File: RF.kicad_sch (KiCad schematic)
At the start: 5 parts, among them U9 SAM-M10Q-00B

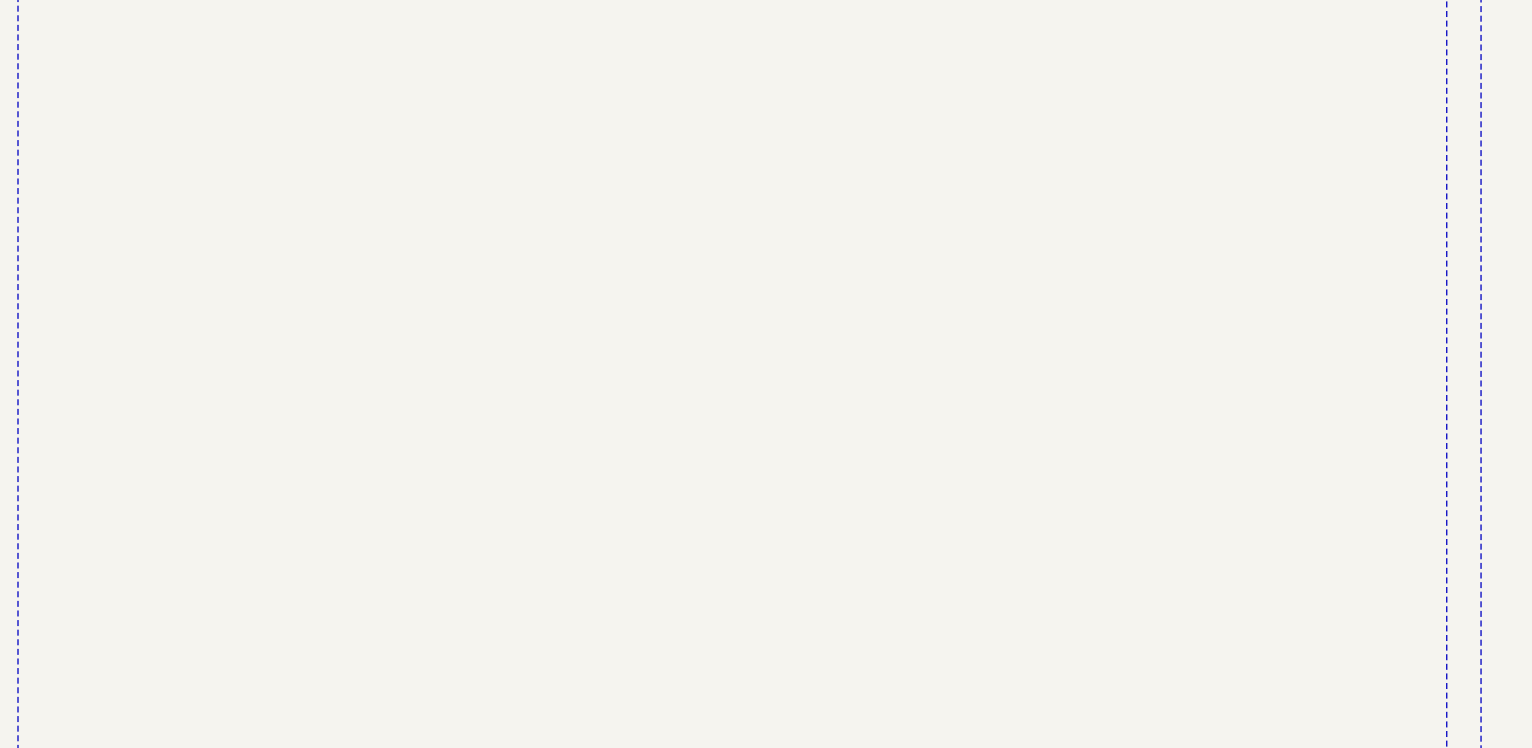
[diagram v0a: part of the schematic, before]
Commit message: added Buzzer, status LEDs
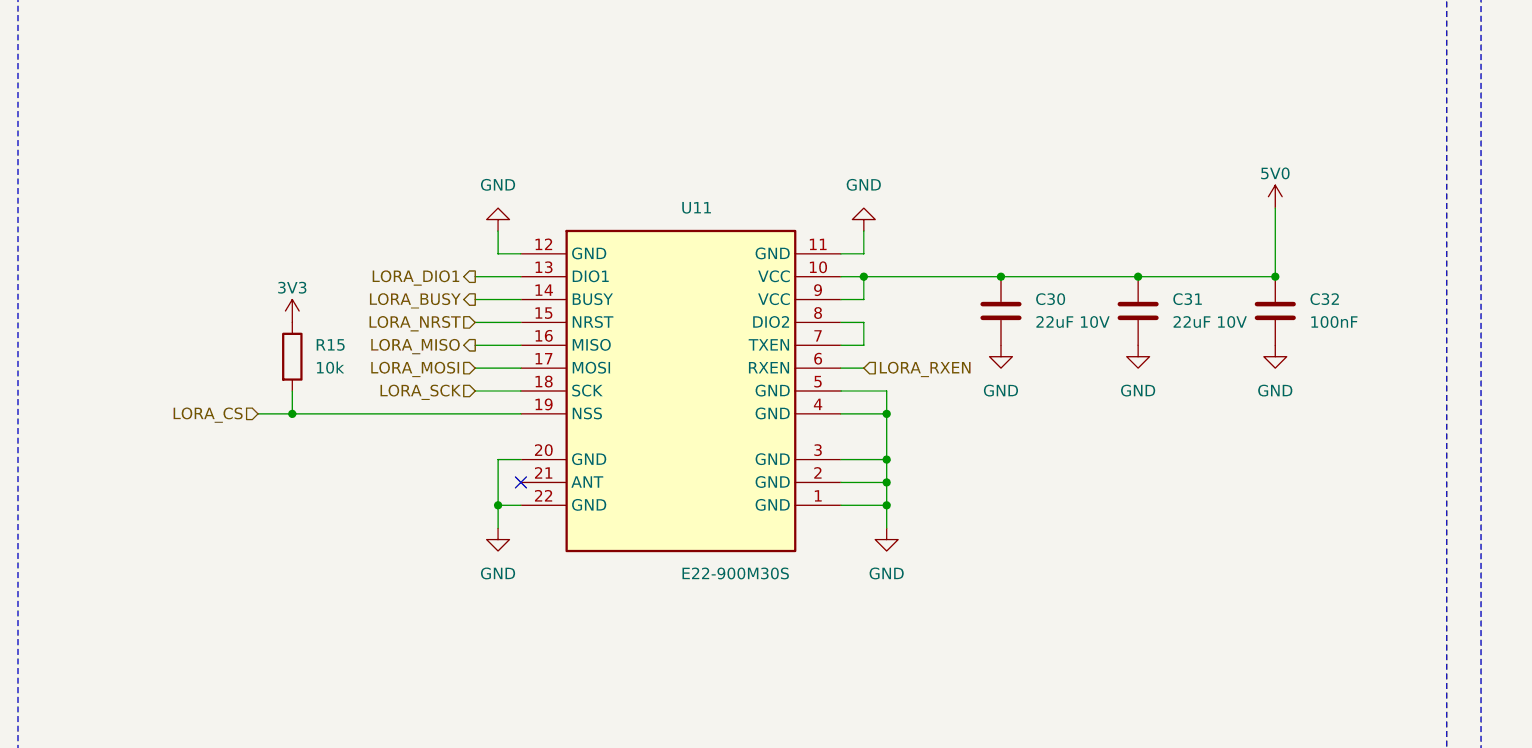
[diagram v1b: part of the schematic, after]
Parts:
- added C30, C31: 22uF 10V, Capacitor_SMD:C_1206_3216Metric, symbol Device:C
- added C32: 100nF, Capacitor_SMD:C_0603_1608Metric, symbol Device:C
- added R15: 10k, Resistor_SMD:R_0603_1608Metric, symbol Device:R
- added U11: E22-900M30S, MyKiCAD:WIRELM-SMD_E22-900M30S, symbol MyKiCAD:E22-900M30S
- TP6: footprint (none) -> TestPoint:TestPoint_Pad_D1.5mm
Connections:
- net 3V3: now also R15.1
- net GND: now also C30.2, C31.2, C32.2, U11.1 (GND), U11.11 (GND), U11.12 (GND), U11.2 (GND), U11.20 (GND), U11.22 (GND), U11.3 (GND), U11.4 (GND), U11.5 (GND)
- new net: U11.7 (TXEN), U11.8 (DIO2)
- new net 5V0: C30.1, C31.1, C32.1, U11.10 (VCC), U11.9 (VCC)
- new net LORA_BUSY: U11.14 (BUSY)
- new net LORA_CS: R15.2, U11.19 (NSS)
- new net LORA_DIO1: U11.13 (DIO1)
- new net LORA_MISO: U11.16 (MISO)
- new net LORA_MOSI: U11.17 (MOSI)
- new net LORA_NRST: U11.15 (NRST)
- new net LORA_RXEN: U11.6 (RXEN)
- new net LORA_SCK: U11.18 (SCK)
- no-connect marks 3 -> 4

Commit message: Battery protection, camera switch, 64MB flash, ERC clean
- Fuse + TVS on battery input, camera load switch (TPS22917)
- Flash to W25Q512JVFIQ (SOIC-16), hand-solder passive footprints
- Power LED, title blocks, U5 footprint, PWR/NC flags (0 ERC)
- Regenerated schematic PDF
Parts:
- C27, C28, C32: footprint Capacitor_SMD:C_0603_1608Metric -> Capacitor_SMD:C_0603_1608Metric_Pad1.08x0.95mm_HandSolder
- C30, C31: footprint Capacitor_SMD:C_1206_3216Metric -> Capacitor_SMD:C_1206_3216Metric_Pad1.33x1.80mm_HandSolder
- FB2: footprint Inductor_SMD:L_0603_1608Metric -> Inductor_SMD:L_0603_1608Metric_Pad1.05x0.95mm_HandSolder
- R15: footprint Resistor_SMD:R_0603_1608Metric -> Resistor_SMD:R_0603_1608Metric_Pad0.98x0.95mm_HandSolder
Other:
- title: (none) -> RF: LoRa Telemetry and GPS
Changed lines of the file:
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@@
 	(generator_version "10.0")
 	(paper "A4")
+	(title_block
+		(title "RF: LoRa Telemetry and GPS")
+		(date "2026-10-23")
+		(comment 1 "Author: Malek Albdoor")
+	)
 	(rectangle
 		(start 15.24 15.24)
@@
 			)
 		)
-		(property "Footprint" "Capacitor_SMD:C_0603_1608Metric"
+		(property "Footprint" "Capacitor_SMD:C_0603_1608Metric_Pad1.08x0.95mm_HandSolder"
 			(at 154.94 90.17 0)
 			(hide yes)
@@
 			)
 		)
-		(property "Footprint" "Capacitor_SMD:C_1206_3216Metric"
+		(property "Footprint" "Capacitor_SMD:C_1206_3216Metric_Pad1.33x1.80mm_HandSolder"
 			(at 139.7 90.17 0)
 			(hide yes)
@@
 			)
 		)
-		(property "Footprint" "Capacitor_SMD:C_1206_3216Metric"
+		(property "Footprint" "Capacitor_SMD:C_1206_3216Metric_Pad1.33x1.80mm_HandSolder"
 			(at 124.46 90.17 0)
 			(hide yes)
@@
 			)
 		)
-		(property "Footprint" "Capacitor_SMD:C_0603_1608Metric"
+		(property "Footprint" "Capacitor_SMD:C_0603_1608Metric_Pad1.08x0.95mm_HandSolder"
 			(at 207.9752 81.28 0)
 			(hide yes)
@@
 			)
 		)
-		(property "Footprint" "Resistor_SMD:R_0603_1608Metric"
+		(property "Footprint" "Resistor_SMD:R_0603_1608Metric_Pad0.98x0.95mm_HandSolder"
 			(at 45.72 95.25 0)
 			(hide yes)
@@
 			)
 		)
-		(property "Footprint" "Capacitor_SMD:C_0603_1608Metric"
+		(property "Footprint" "Capacitor_SMD:C_0603_1608Metric_Pad1.08x0.95mm_HandSolder"
 			(at 221.9452 81.28 0)
 			(hide yes)
@@
 			)
 		)
-		(property "Footprint" "Inductor_SMD:L_0603_1608Metric"
+		(property "Footprint" "Inductor_SMD:L_0603_1608Metric_Pad1.05x0.95mm_HandSolder"
 			(at 231.14 69.85 0)
 			(hide yes)
